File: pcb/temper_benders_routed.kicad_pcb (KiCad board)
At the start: 4 copper layers, 120 x 170 mm, 33 parts, among them Q1 IKW40N120H3, Q2 IKW40N120H3

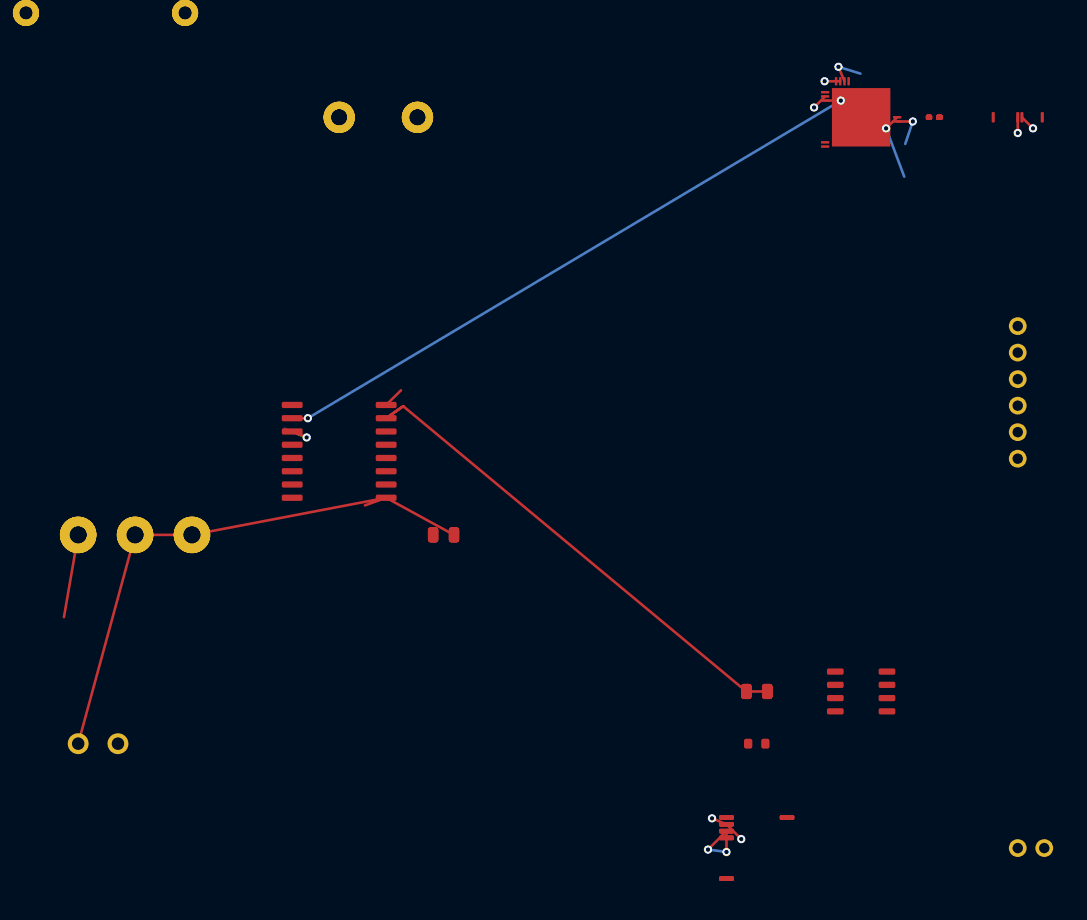
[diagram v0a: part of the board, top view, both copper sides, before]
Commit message: checkpoint: before ExactGeometryRouter Phase 1-3 improvements
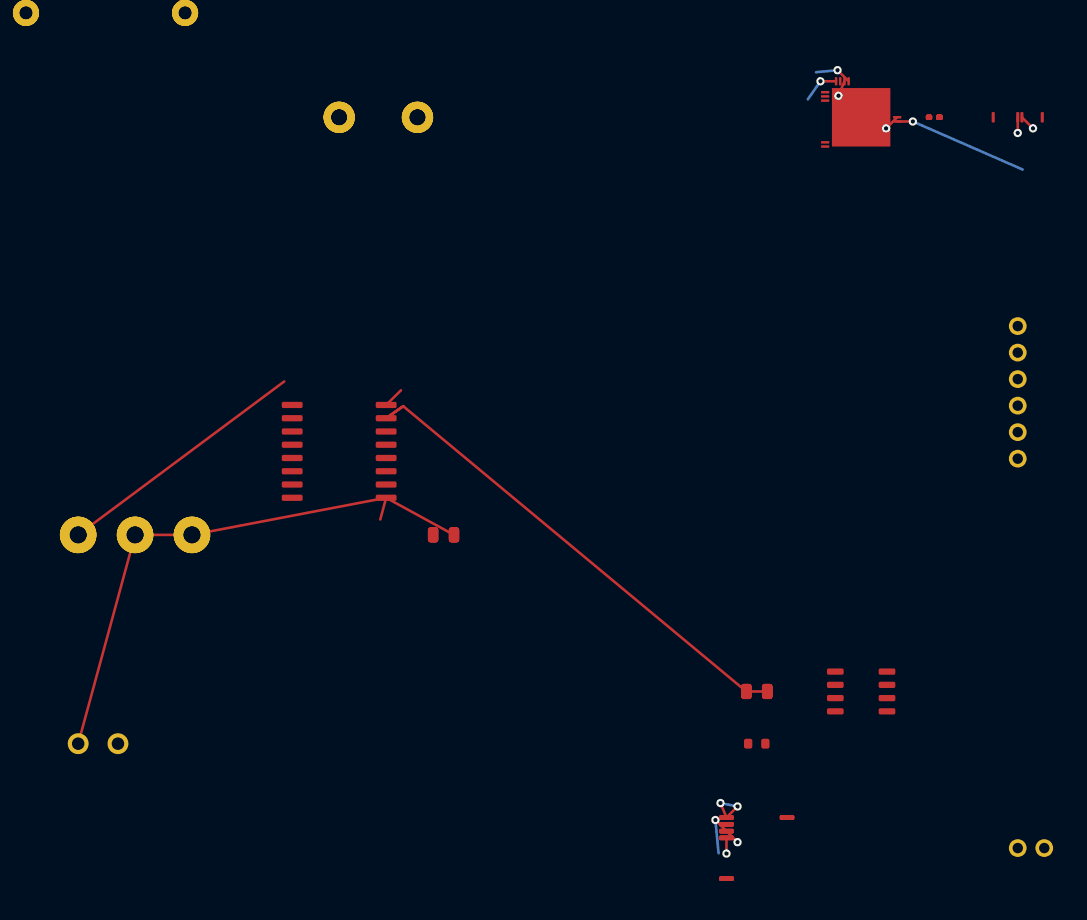
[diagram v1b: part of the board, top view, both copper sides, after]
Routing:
- net PWM_H: track 62.4 -> 0.00 mm, vias 2 -> 0
- net GATE_H: track 56.7 -> 73.4 mm
- net SPI_MOSI: track 9.28 -> 0.00 mm, vias 3 -> 0
- net USB_D-: track 5.27 -> 14.5 mm
- net SPI_CLK: track 0.00 -> 8.27 mm, vias 0 -> 3
- net PWM_L: track 5.27 -> 0.00 mm, vias 2 -> 0
- net SPI_CS_TEMP: track 0.00 -> 5.08 mm, vias 0 -> 2
- net USB_D+: track 7.94 -> 5.15 mm
- net SPI_MISO: track 9.99 -> 12.2 mm
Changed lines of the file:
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@@
   (gr_line (start 35 48) (end 0 48) (layer "Edge.Cuts") (width 0.15))
   (gr_line (start 0 48) (end 0 0) (layer "Edge.Cuts") (width 0.15))
-  (segment (start 20 125) (end 18.63615038335621 132.88312228415717) (width 0.25) (layer "F.Cu") (net 11))
+  (segment (start 20 125) (end 39.73914706271651 110.30338833710674) (width 0.25) (layer "F.Cu") (net 11))
   (segment (start 51.13418729462423 112.67199007545958) (end 49.5 113.825) (width 0.25) (layer "F.Cu") (net 11))
   (segment (start 49.5 113.825) (end 51.13418729462423 112.67199007545958) (width 0.25) (layer "F.Cu") (net 11))
   (segment (start 51.13418729462423 112.67199007545958) (end 84 140) (width 0.25) (layer "F.Cu") (net 11))
   (segment (start 84 140) (end 86 140) (width 0.25) (layer "F.Cu") (net 11))
-  (segment (start 91.55 83.4) (end 93.05 83.4) (width 0.25) (layer "F.Cu") (net 13))
-  (segment (start 40.5 113.825) (end 42.0 113.825) (width 0.25) (layer "F.Cu") (net 13))
-  (segment (start 42.0 113.825) (end 93.05 83.4) (width 0.25) (layer "B.Cu") (net 13))
-  (segment (start 91.55 83) (end 90.48933982822018 84.06066017177982) (width 0.25) (layer "F.Cu") (net 14))
-  (segment (start 40.5 115.095) (end 41.88581929876693 115.66902514854763) (width 0.25) (layer "F.Cu") (net 14))
-  (segment (start 41.88581929876693 115.66902514854763) (end 39.76986449899469 114.84591841345916) (width 0.25) (layer "B.Cu") (net 14))
-  (segment (start 82.1 152.725) (end 83.51421356237309 154.1392135623731) (width 0.25) (layer "F.Cu") (net 22))
-  (segment (start 82.1 152.725) (end 80.71418070123306 152.15097485145236) (width 0.25) (layer "F.Cu") (net 22))
-  (segment (start 93 81.55) (end 91.5 81.55) (width 0.25) (layer "F.Cu") (net 22))
-  (segment (start 91.5 81.55) (end 90.05050851131982 80.07127044284925) (width 0.25) (layer "In1.Cu") (net 22))
-  (segment (start 80.71418070123306 152.15097485145236) (end 80.9899059381488 154.33901445417527) (width 0.25) (layer "In1.Cu") (net 22))
-  (segment (start 82.1 153.375) (end 80.33223304703363 155.14276695296638) (width 0.25) (layer "F.Cu") (net 23))
-  (segment (start 82.1 153.375) (end 82.1 155.375) (width 0.25) (layer "F.Cu") (net 23))
-  (segment (start 93.4 81.55) (end 92.82597485145237 80.16418070123306) (width 0.25) (layer "F.Cu") (net 23))
-  (segment (start 92.82597485145237 80.16418070123306) (end 94.93620654816144 80.81660500718924) (width 0.25) (layer "B.Cu") (net 23))
-  (segment (start 82.1 155.375) (end 80.33223304703363 155.14276695296638) (width 0.25) (layer "B.Cu") (net 23))
+  (segment (start 82.1 153.375) (end 81.03933982822018 152.31433982822017) (width 0.25) (layer "F.Cu") (net 23))
+  (segment (start 82.1 153.375) (end 83.16066017177981 154.43566017177983) (width 0.25) (layer "F.Cu") (net 23))
+  (segment (start 93.4 81.55) (end 92.82597485145237 82.93581929876693) (width 0.25) (layer "F.Cu") (net 23))
+  (segment (start 92.82597485145237 82.93581929876693) (end 92.98805467744143 87.4193243004673) (width 0.25) (layer "B.Cu") (net 23))
+  (segment (start 81.03933982822018 152.31433982822017) (end 81.34319264423777 155.4977888498306) (width 0.25) (layer "B.Cu") (net 23))
+  (segment (start 82.1 154.025) (end 82.1 155.525) (width 0.25) (layer "F.Cu") (net 24))
+  (segment (start 93.8 81.55) (end 92.73933982822018 80.48933982822018) (width 0.25) (layer "F.Cu") (net 24))
+  (segment (start 92.73933982822018 80.48933982822018) (end 90.67003741482948 80.67973408176974) (width 0.25) (layer "B.Cu") (net 24))
   (segment (start 110.4 85) (end 111.46066017177982 86.06066017177982) (width 0.25) (layer "F.Cu") (net 26))
   (segment (start 98.45 85.4) (end 99.95 85.4) (width 0.25) (layer "F.Cu") (net 26))
-  (segment (start 99.95 85.4) (end 99.22142287303683 87.55105509414584) (width 0.25) (layer "B.Cu") (net 26))
+  (segment (start 99.95 85.4) (end 110.46317194273891 90.00121719380866) (width 0.25) (layer "B.Cu") (net 26))
   (segment (start 30.9 125) (end 25.45 125) (width 0.25) (layer "F.Cu") (net 10))
   (segment (start 30.9 125) (end 49.5 121.445) (width 0.25) (layer "F.Cu") (net 10))
   (segment (start 49.5 121.445) (end 56 125) (width 0.25) (layer "F.Cu") (net 10))
-  (segment (start 49.5 121.445) (end 47.46878704046584 122.17446949181743) (width 0.25) (layer "F.Cu") (net 10))
+  (segment (start 49.5 121.445) (end 48.937799356883076 123.52871837428928) (width 0.25) (layer "F.Cu") (net 10))
   (segment (start 50.92288222136117 111.14950856134436) (end 49.5 112.555) (width 0.25) (layer "F.Cu") (net 10))
   (segment (start 25.45 125) (end 20 145) (width 0.25) (layer "F.Cu") (net 10))
+  (segment (start 82.1 152.075) (end 83.16066017177981 151.01433982822016) (width 0.25) (layer "F.Cu") (net 21))
+  (segment (start 82.1 152.075) (end 81.52597485145236 150.68918070123306) (width 0.25) (layer "F.Cu") (net 21))
+  (segment (start 92.6 81.55) (end 91.1 81.55) (width 0.25) (layer "F.Cu") (net 21))
+  (segment (start 91.1 81.55) (end 89.89237752038137 83.27675775395235) (width 0.25) (layer "B.Cu") (net 21))
+  (segment (start 81.52597485145236 150.68918070123306) (end 83.16066017177981 151.01433982822016) (width 0.25) (layer "B.Cu") (net 21))
   (segment (start 110 85) (end 110.0 86.5) (width 0.25) (layer "F.Cu") (net 25))
   (segment (start 98.45 85) (end 97.38933982822019 86.06066017177982) (width 0.25) (layer "F.Cu") (net 25))
-  (segment (start 97.38933982822019 86.06066017177982) (end 99.13179109754788 90.68769267258774) (width 0.25) (layer "B.Cu") (net 25))
+  (segment (start 97.38933982822019 86.06066017177982) (end 97.46612661191168 83.9120751716919) (width 0.25) (layer "B.Cu") (net 25))
   (segment (start 15 35) (end 30.240000000000002 75) (width 0.25) (layer "F.Cu") (net 20))
-  (via (at 42.0 113.825) (size 0.8) (drill 0.4) (layers "F.Cu" "B.Cu") (net 13))
-  (via (at 93.05 83.4) (size 0.8) (drill 0.4) (layers "F.Cu" "B.Cu") (net 13))
-  (via (at 41.88581929876693 115.66902514854763) (size 0.8) (drill 0.4) (layers "F.Cu" "B.Cu") (net 14))
-  (via (at 90.48933982822018 84.06066017177982) (size 0.8) (drill 0.4) (layers "F.Cu" "B.Cu") (net 14))
-  (via (at 91.5 81.55) (size 0.8) (drill 0.4) (layers "F.Cu" "B.Cu") (net 22))
-  (via (at 80.71418070123306 152.15097485145236) (size 0.8) (drill 0.4) (layers "F.Cu" "B.Cu") (net 22))
-  (via (at 83.51421356237309 154.1392135623731) (size 0.8) (drill 0.4) (layers "F.Cu" "B.Cu") (net 22))
-  (via (at 92.82597485145237 80.16418070123306) (size 0.8) (drill 0.4) (layers "F.Cu" "B.Cu") (net 23))
-  (via (at 82.1 155.375) (size 0.8) (drill 0.4) (layers "F.Cu" "B.Cu") (net 23))
-  (via (at 80.33223304703363 155.14276695296638) (size 0.8) (drill 0.4) (layers "F.Cu" "B.Cu") (net 23))
+  (via (at 92.82597485145237 82.93581929876693) (size 0.8) (drill 0.4) (layers "F.Cu" "B.Cu") (net 23))
+  (via (at 83.16066017177981 154.43566017177983) (size 0.8) (drill 0.4) (layers "F.Cu" "B.Cu") (net 23))
+  (via (at 81.03933982822018 152.31433982822017) (size 0.8) (drill 0.4) (layers "F.Cu" "B.Cu") (net 23))
+  (via (at 92.73933982822018 80.48933982822018) (size 0.8) (drill 0.4) (layers "F.Cu" "B.Cu") (net 24))
+  (via (at 82.1 155.525) (size 0.8) (drill 0.4) (layers "F.Cu" "B.Cu") (net 24))
   (via (at 99.95 85.4) (size 0.8) (drill 0.4) (layers "F.Cu" "B.Cu") (net 26))
   (via (at 111.46066017177982 86.06066017177982) (size 0.8) (drill 0.4) (layers "F.Cu" "B.Cu") (net 26))
+  (via (at 91.1 81.55) (size 0.8) (drill 0.4) (layers "F.Cu" "B.Cu") (net 21))
+  (via (at 81.52597485145236 150.68918070123306) (size 0.8) (drill 0.4) (layers "F.Cu" "B.Cu") (net 21))
+  (via (at 83.16066017177981 151.01433982822016) (size 0.8) (drill 0.4) (layers "F.Cu" "B.Cu") (net 21))
   (via (at 97.38933982822019 86.06066017177982) (size 0.8) (drill 0.4) (layers "F.Cu" "B.Cu") (net 25))
   (via (at 110.0 86.5) (size 0.8) (drill 0.4) (layers "F.Cu" "B.Cu") (net 25))
